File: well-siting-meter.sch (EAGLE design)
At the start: 46 parts, among them J2 7805, T1 MOSFET-NCHANNELFQP30N06L, U1 LCD-16X2NOHOLES, U2 ARDUINO_PRO_MINI, U3 EC2, U4 EC2, U5 AD623, U6 AD623, U7 MAX1771

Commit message: prep for mfg
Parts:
- C1: value 100uF, 35V -> 100uF
- C4: value 4u7, 250V -> 4u7
- C6: value 0.1uf, 250V -> 0.1uf
- L1: value MURATA1400 -> 22uH; device murata1400:MURATA1400 -> misc:WE-FAMI; PN 811-2633-ND -> (none)
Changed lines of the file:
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@@
 <grid distance="0.1" unitdist="inch" unit="inch" style="lines" multiple="1" display="no" altdistance="0.01" altunitdist="inch" altunit="inch"/>
 <layers>
-<layer number="1" name="Top" color="4" fill="1" visible="yes" active="no"/>
-<layer number="16" name="Bottom" color="1" fill="1" visible="yes" active="no"/>
-<layer number="17" name="Pads" color="2" fill="1" visible="yes" active="no"/>
-<layer number="18" name="Vias" color="2" fill="1" visible="yes" active="no"/>
-<layer number="19" name="Unrouted" color="6" fill="1" visible="yes" active="no"/>
-<layer number="20" name="Dimension" color="15" fill="1" visible="yes" active="no"/>
-<layer number="21" name="tPlace" color="7" fill="1" visible="yes" active="no"/>
-<layer number="22" name="bPlace" color="7" fill="1" visible="yes" active="no"/>
-<layer number="23" name="tOrigins" color="15" fill="1" visible="yes" active="no"/>
-<layer number="24" name="bOrigins" color="15" fill="1" visible="yes" active="no"/>
-<layer number="25" name="tNames" color="7" fill="1" visible="yes" active="no"/>
-<layer number="26" name="bNames" color="7" fill="1" visible="yes" active="no"/>
-<layer number="27" name="tValues" color="7" fill="1" visible="yes" active="no"/>
-<layer number="28" name="bValues" color="7" fill="1" visible="yes" active="no"/>
+<layer number="1" name="Top" color="4" fill="1" visible="no" active="no"/>
+<layer number="16" name="Bottom" color="1" fill="1" visible="no" active="no"/>
+<layer number="17" name="Pads" color="2" fill="1" visible="no" active="no"/>
+<layer number="18" name="Vias" color="2" fill="1" visible="no" active="no"/>
+<layer number="19" name="Unrouted" color="6" fill="1" visible="no" active="no"/>
+<layer number="20" name="Dimension" color="15" fill="1" visible="no" active="no"/>
+<layer number="21" name="tPlace" color="7" fill="1" visible="no" active="no"/>
+<layer number="22" name="bPlace" color="7" fill="1" visible="no" active="no"/>
+<layer number="23" name="tOrigins" color="15" fill="1" visible="no" active="no"/>
+<layer number="24" name="bOrigins" color="15" fill="1" visible="no" active="no"/>
+<layer number="25" name="tNames" color="7" fill="1" visible="no" active="no"/>
+<layer number="26" name="bNames" color="7" fill="1" visible="no" active="no"/>
+<layer number="27" name="tValues" color="7" fill="1" visible="no" active="no"/>
+<layer number="28" name="bValues" color="7" fill="1" visible="no" active="no"/>
 <layer number="29" name="tStop" color="7" fill="3" visible="no" active="no"/>
 <layer number="30" name="bStop" color="7" fill="6" visible="no" active="no"/>
@@
 <layer number="35" name="tGlue" color="7" fill="4" visible="no" active="no"/>
 <layer number="36" name="bGlue" color="7" fill="5" visible="no" active="no"/>
-<layer number="37" name="tTest" color="7" fill="1" visible="yes" active="no"/>
-<layer number="38" name="bTest" color="7" fill="1" visible="yes" active="no"/>
+<layer number="37" name="tTest" color="7" fill="1" visible="no" active="no"/>
+<layer number="38" name="bTest" color="7" fill="1" visible="no" active="no"/>
 <layer number="39" name="tKeepout" color="4" fill="11" visible="no" active="no"/>
 <layer number="40" name="bKeepout" color="1" fill="11" visible="no" active="no"/>
@@
 <layer number="44" name="Drills" color="7" fill="1" visible="no" active="no"/>
 <layer number="45" name="Holes" color="7" fill="1" visible="no" active="no"/>
-<layer number="46" name="Milling" color="3" fill="1" visible="yes" active="no"/>
-<layer number="47" name="Measures" color="7" fill="1" visible="yes" active="no"/>
-<layer number="48" name="Document" color="7" fill="1" visible="yes" active="no"/>
-<layer number="49" name="Reference" color="7" fill="1" visible="yes" active="no"/>
-<layer number="50" name="dxf" color="7" fill="1" visible="yes" active="no"/>
-<layer number="51" name="tDocu" color="7" fill="1" visible="yes" active="no"/>
-<layer number="52" name="bDocu" color="7" fill="1" visible="yes" active="no"/>
-<layer number="53" name="tGND_GNDA" color="7" fill="9" visible="yes" active="no"/>
-<layer number="54" name="bGND_GNDA" color="1" fill="9" visible="yes" active="no"/>
-<layer number="56" name="wert" color="7" fill="1" visible="yes" active="no"/>
-<layer number="57" name="tCAD" color="7" fill="1" visible="yes" active="no"/>
-<layer number="59" name="tCarbon" color="7" fill="1" visible="yes" active="no"/>
-<layer number="60" name="bCarbon" color="7" fill="1" visible="yes" active="no"/>
+<layer number="46" name="Milling" color="3" fill="1" visible="no" active="no"/>
+<layer number="47" name="Measures" color="7" fill="1" visible="no" active="no"/>
+<layer number="48" name="Document" color="7" fill="1" visible="no" active="no"/>
+<layer number="49" name="Reference" color="7" fill="1" visible="no" active="no"/>
+<layer number="50" name="dxf" color="7" fill="1" visible="no" active="no"/>
+<layer number="51" name="tDocu" color="7" fill="1" visible="no" active="no"/>
+<layer number="52" name="bDocu" color="7" fill="1" visible="no" active="no"/>
+<layer number="53" name="tGND_GNDA" color="7" fill="9" visible="no" active="no"/>
+<layer number="54" name="bGND_GNDA" color="1" fill="9" visible="no" active="no"/>
+<layer number="56" name="wert" color="7" fill="1" visible="no" active="no"/>
+<layer number="57" name="tCAD" color="7" fill="1" visible="no" active="no"/>
+<layer number="59" name="tCarbon" color="7" fill="1" visible="no" active="no"/>
+<layer number="60" name="bCarbon" color="7" fill="1" visible="no" active="no"/>
 <layer number="90" name="Modules" color="5" fill="1" visible="yes" active="yes"/>
 <layer number="91" name="Nets" color="2" fill="1" visible="yes" active="yes"/>
@@
 <attribute name="PN" value="SW406-ND"/>
 </part>
-<part name="C1" library="SparkFun-Passives" deviceset="CAP_POL" device="PTH1" value="100uF, 35V">
+<part name="C1" library="SparkFun-Passives" deviceset="CAP_POL" device="PTH1" value="100uF">
 <attribute name="PN" value="1572-1306-ND"/>
 </part>
@@
 <attribute name="PN" value="1.00MXBK-ND"/>
 </part>
-<part name="C6" library="SparkFun-Passives" deviceset="CAP" device="PTH" value="0.1uf, 250V">
+<part name="C6" library="SparkFun-Passives" deviceset="CAP" device="PTH" value="0.1uf">
 <attribute name="PN" value="445-173449-1-ND"/>
 </part>
-<part name="C4" library="SparkFun-Passives" deviceset="CAP_POL" device="PTH1" value="4u7, 250V">
+<part name="C4" library="SparkFun-Passives" deviceset="CAP_POL" device="PTH1" value="4u7">
 <attribute name="PN" value="399-6091-ND"/>
 </part>
@@
 <part name="GND15" library="SparkFun-Aesthetics" deviceset="GND" device=""/>
 <part name="TM1" library="adafruit" deviceset="TRIM" device="3386"/>
-<part name="L1" library="murata1400" deviceset="MURATA1400" device="">
-<attribute name="PN" value="811-2633-ND"/>
-</part>
+<part name="L1" library="misc" deviceset="WE-FAMI" device="" value="22uH"/>
 </parts>
 <sheets>
@@
 <instance part="GND15" gate="1" x="223.52" y="66.04"/>
 <instance part="TM1" gate="G$1" x="101.6" y="58.42" rot="R180"/>
-<instance part="L1" gate="G$1" x="73.66" y="83.82" rot="R90">
-<attribute name="PN" x="73.66" y="83.82" size="1.778" layer="96" rot="R90" display="off"/>
-</instance>
+<instance part="L1" gate="G$1" x="73.66" y="83.82" rot="R90"/>
 </instances>
 <busses>
@@
 <segment>
 <pinref part="R7" gate="G$1" pin="2"/>
-<wire x1="190.5" y1="127" x2="187.96" y2="127" width="0.1524" layer="91"/>
-<wire x1="187.96" y1="127" x2="182.88" y2="127" width="0.1524" layer="91"/>
 <wire x1="182.88" y1="127" x2="182.88" y2="124.46" width="0.1524" layer="91"/>
 <pinref part="GND10" gate="1" pin="GND"/>
 <wire x1="182.88" y1="127" x2="177.8" y2="127" width="0.1524" layer="91"/>
 <wire x1="177.8" y1="127" x2="177.8" y2="124.46" width="0.1524" layer="91"/>
+<junction x="182.88" y="127"/>
 <pinref part="U5" gate="G$1" pin="-IN"/>
-<junction x="187.96" y="127"/>
+<wire x1="182.88" y1="127" x2="187.96" y2="127" width="0.1524" layer="91"/>
 </segment>
 <segment>
@@
 <pinref part="U2" gate="G$1" pin="*9"/>
 <wire x1="134.62" y1="106.68" x2="127" y2="106.68" width="0.1524" layer="91"/>
+<label x="127" y="106.68" size="1.778" layer="95"/>
 </segment>
 </net>
@@
 <pinref part="U2" gate="G$1" pin="8"/>
 <wire x1="134.62" y1="109.22" x2="127" y2="109.22" width="0.1524" layer="91"/>
+<label x="127" y="109.22" size="1.778" layer="95"/>
 </segment>
 </net>
@@
 <wire x1="223.52" y1="121.92" x2="233.68" y2="121.92" width="0.1524" layer="91"/>
 <label x="226.06" y="121.92" size="1.778" layer="95"/>
+<junction x="223.52" y="121.92"/>
 </segment>
 </net>
@@
 <pinref part="U2" gate="G$1" pin="*10"/>
 <wire x1="157.48" y1="106.68" x2="165.1" y2="106.68" width="0.1524" layer="91"/>
+<label x="157.48" y="106.68" size="1.778" layer="95"/>
 </segment>
 </net>
@@
 <wire x1="157.48" y1="109.22" x2="165.1" y2="109.22" width="0.1524" layer="91"/>
 <label x="157.48" y="109.22" size="1.778" layer="95"/>
-<label x="157.48" y="106.68" size="1.778" layer="95"/>
 </segment>
 </net>
@@
 <pinref part="U2" gate="G$1" pin="4"/>
 <wire x1="134.62" y1="119.38" x2="127" y2="119.38" width="0.1524" layer="91"/>
+<label x="127" y="119.38" size="1.778" layer="95"/>
 </segment>
 <segment>
@@
 <pinref part="U2" gate="G$1" pin="*5"/>
 <wire x1="134.62" y1="116.84" x2="127" y2="116.84" width="0.1524" layer="91"/>
-</segment>
-<segment>
+<label x="127" y="116.84" size="1.778" layer="95"/>
+</segment>
+<segment>

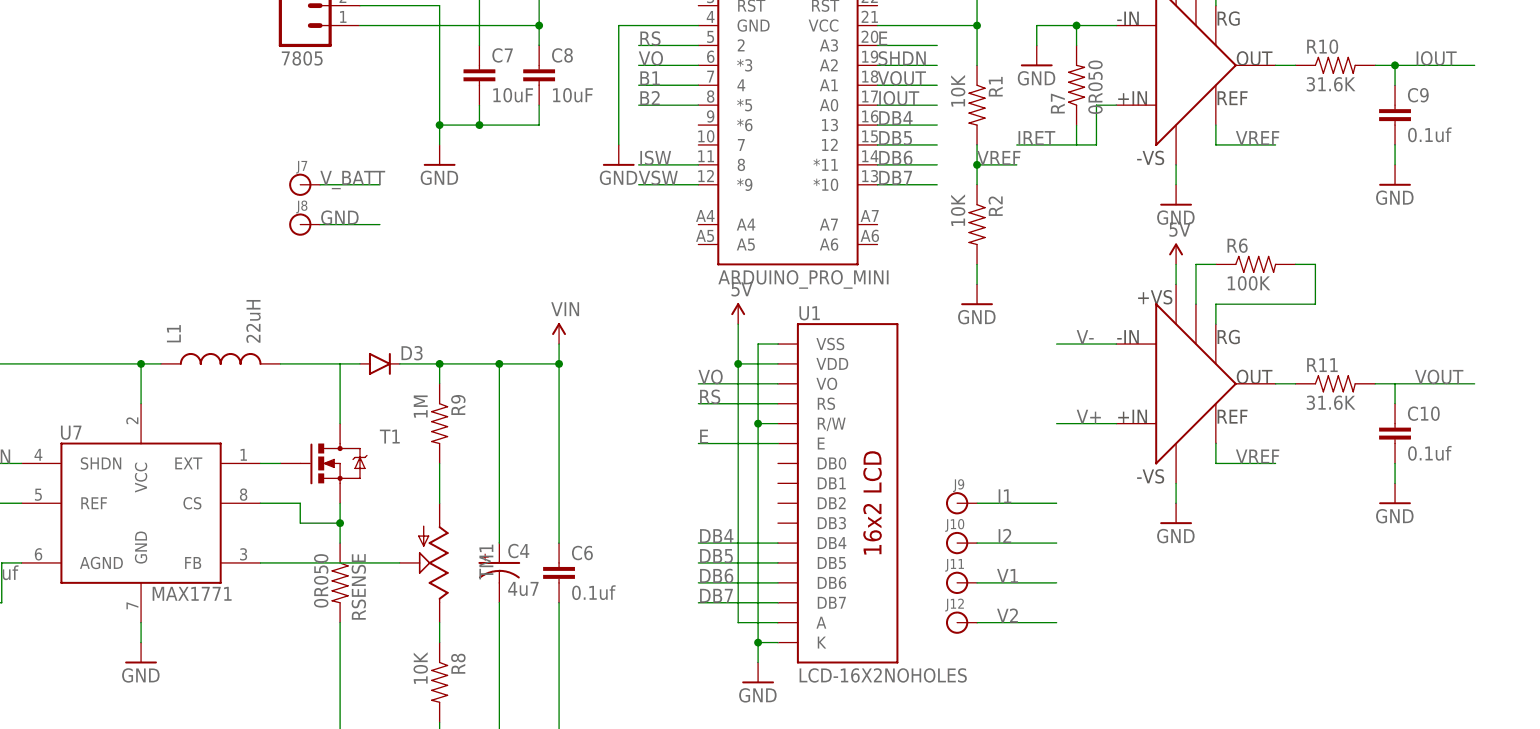
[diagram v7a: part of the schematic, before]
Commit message: adding optional 2nd inductor, more mfg prep
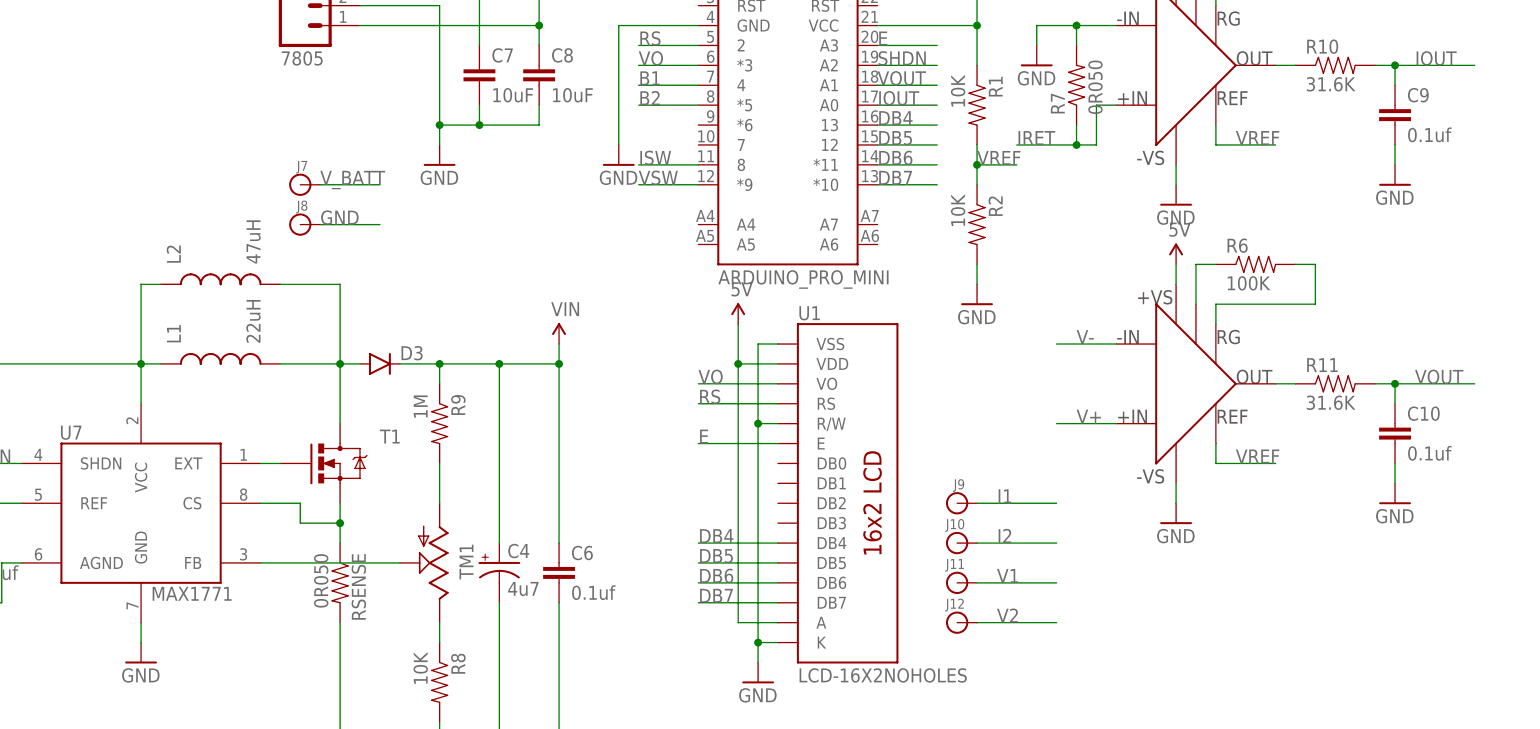
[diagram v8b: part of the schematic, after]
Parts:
- added L2: 47uH, murata1400:MURATA1400
- L1: PN (none) -> 732-7163-ND
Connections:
- net N$9: now also L2.2
- net V_BATT: now also L2.1
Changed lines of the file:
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@@
 <part name="GND15" library="SparkFun-Aesthetics" deviceset="GND" device=""/>
 <part name="TM1" library="adafruit" deviceset="TRIM" device="3386"/>
-<part name="L1" library="misc" deviceset="WE-FAMI" device="" value="22uH"/>
+<part name="L1" library="misc" deviceset="WE-FAMI" device="" value="22uH">
+<attribute name="PN" value="732-7163-ND"/>
+</part>
+<part name="L2" library="murata1400" deviceset="MURATA1400" device="" value="47uH">
+<attribute name="PN" value="811-2633-ND"/>
+</part>
 </parts>
 <sheets>
@@
 <instance part="GND14" gate="1" x="223.52" y="106.68"/>
 <instance part="GND15" gate="1" x="223.52" y="66.04"/>
-<instance part="TM1" gate="G$1" x="101.6" y="58.42" rot="R180"/>
-<instance part="L1" gate="G$1" x="73.66" y="83.82" rot="R90"/>
+<instance part="TM1" gate="G$1" x="101.6" y="58.42" smashed="yes" rot="R180">
+<attribute name="NAME" x="104.14" y="60.96" size="1.778" layer="95" rot="R270"/>
+<attribute name="VALUE" x="104.14" y="60.96" size="1.778" layer="96" rot="R270"/>
+</instance>
+<instance part="L1" gate="G$1" x="73.66" y="83.82" rot="R90">
+<attribute name="PN" x="73.66" y="83.82" size="1.778" layer="96" rot="R90" display="off"/>
+</instance>
+<instance part="L2" gate="G$1" x="73.66" y="93.98" rot="R90">
+<attribute name="PN" x="73.66" y="93.98" size="1.778" layer="96" rot="R90" display="off"/>
+</instance>
 </instances>
 <busses>
@@
 <wire x1="182.88" y1="114.3" x2="182.88" y2="111.76" width="0.1524" layer="91"/>
 <label x="175.26" y="111.76" size="1.778" layer="95"/>
+<junction x="182.88" y="111.76"/>
 </segment>
 </net>
@@
 <pinref part="R11" gate="G$1" pin="2"/>
 <wire x1="223.52" y1="81.28" x2="220.98" y2="81.28" width="0.1524" layer="91"/>
+<junction x="223.52" y="81.28"/>
 </segment>
 </net>
@@
 <wire x1="25.4" y1="83.82" x2="25.4" y2="86.36" width="0.1524" layer="91"/>
 <pinref part="L1" gate="G$1" pin="1"/>
+<wire x1="63.5" y1="83.82" x2="63.5" y2="93.98" width="0.1524" layer="91"/>
+<pinref part="L2" gate="G$1" pin="1"/>
+<wire x1="63.5" y1="93.98" x2="66.04" y2="93.98" width="0.1524" layer="91"/>
 </segment>
 </net>
@@
 <wire x1="88.9" y1="83.82" x2="91.44" y2="83.82" width="0.1524" layer="91"/>
 <pinref part="L1" gate="G$1" pin="2"/>
-</segment>
-</net>
+<junction x="88.9" y="83.82"/>
+<pinref part="L2" gate="G$1" pin="2"/>
+<wire x1="81.28" y1="93.98" x2="88.9" y2="93.98" width="0.1524" layer="91"/>
+<wire x1="88.9" y1="93.98" x2="88.9" y2="83.82" width="0.1524" layer="91"/>
+</segment>
+</net>
